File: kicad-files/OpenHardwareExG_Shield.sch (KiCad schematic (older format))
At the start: 196 parts, among them K1 CONN_3, P1 CONN_1, P10 CONN_10X2, P11 CONN_1, P12 CONN_1, P13 CONN_1, P14 CONN_1, P15 CONN_1, P16 CONN_1, P17 CONN_1, P18 CONN_1, P19 ARDUINO_SHIELD, P2 CONN_1, P20 CONN_3X2, P21 CONN_3X2, P22 CONN_4, P23 CONN_1, P24 CONN_1, P25 CONN_1, P26 CONN_1, P27 CONN_1, P28 CONN_1, P29 CONN_1, P3 CONN_1, P30 CONN_1, P31 CONN_1, P32 CONN_1, P33 CONN_1, P34 CONN_1, P35 CONN_1, P36 CONN_1, P37 CONN_1, P38 CONN_1, P39 CONN_1, P4 CONN_1, P40 CONN_1, P41 CONN_1, P42 CONN_1, P43 CONN_1, P44 CONN_1, P45 CONN_1, P46 CONN_1, P47 CONN_1, P48 CONN_1, P49 CONN_1, P5 CONN_1, P50 CONN_1, P51 CONN_1, P52 CONN_1, P53 CONN_1, P54 CONN_1, P55 CONN_1, P6 CONN_1, P7 CONN_1, P8 CONN_1, P9 CONN_1, U1 ADS1299, U2 BT1308W-600D, U3 TL431BIDBZR, U4 NI, U5 ADUM6000, U6 SI8663, U7 74LS02, U8 74LS00, U9 74LS125

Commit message: starting to choose footprints
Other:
- note added: "Analog Test Points"
- moved on the sheet: P1, P11, P12, P13, P14, P15, P16, P17, P18, P2, P3, P4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

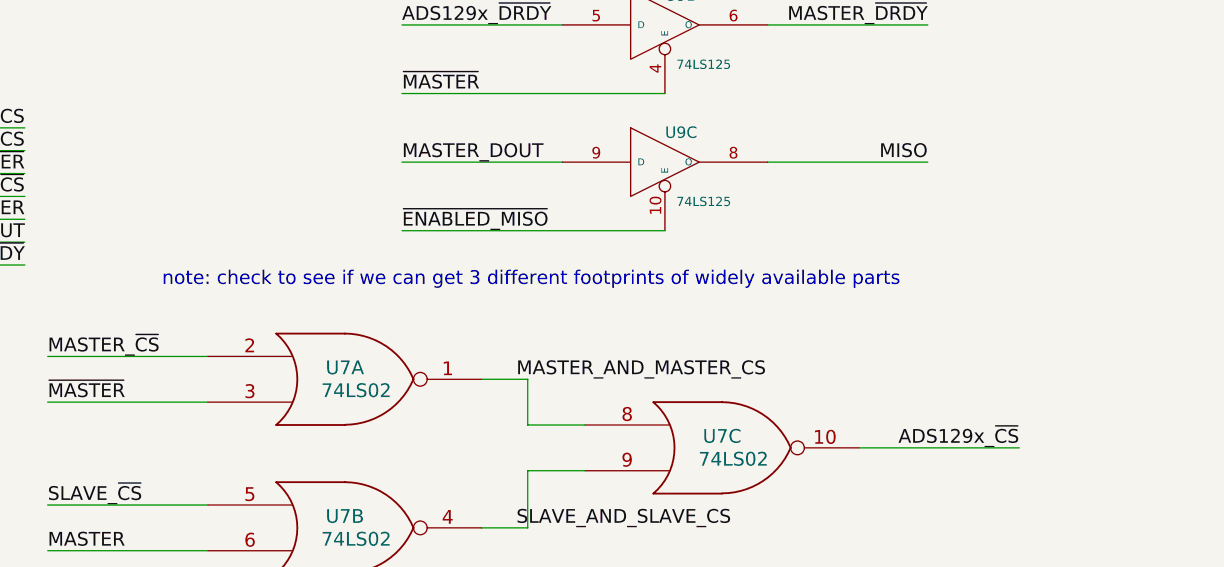
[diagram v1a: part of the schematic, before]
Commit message: add footprints for SMD headers and pogopads
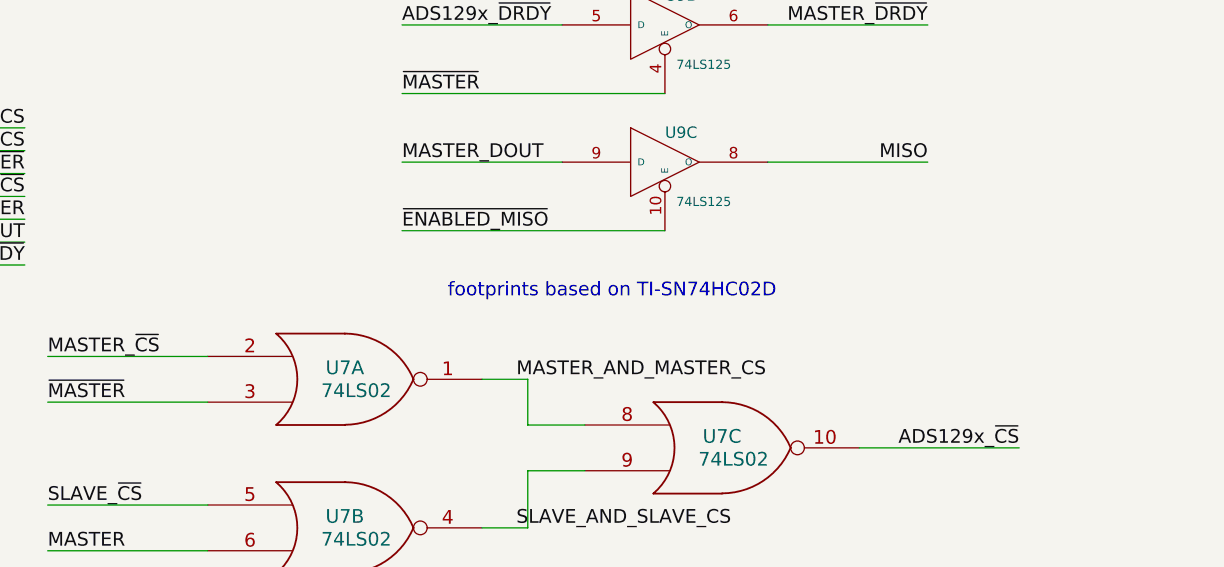
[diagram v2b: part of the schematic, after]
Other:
- note added: "footprints based on TI-SN74HC02D"
- note removed: "note: check to see if we can get 3 different footprints of widely available parts"
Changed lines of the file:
@@
 	1    0    0    -1
 $EndComp
-Text Notes 27600 8200 0    60   ~ 0
-note: check to see if we can get 3 different footprints of widely available parts
 $Comp
 L VCC #PWR069
@@
 Text Notes 23750 9550 2    60   ~ 0
 Analog Test Points
+Text Notes 28850 8250 0    60   ~ 0
+footprints based on TI-SN74HC02D
 $EndSCHEMATC

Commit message: add footprints to schematics
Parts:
- C1, C10, C11, C12, C13, C14, C15, C16, C17, C18, C19, C2, C20, C21, C22, C23, C24, C25, C26, C27, C28, C29, C3, C30, C31, C32, C33, C34, C4, C5, C6, C7, C8, C9, R1, R10, R11, R12, R13, R14, R15, R16, R17, R18, R19, R2, R20, R21, R22, R23, R24, R25, R26, R27, R28, R29, R3, R30, R31, R32, R33, R34, R4, R5, R6, R7, R8, R9: footprint SM0603 -> SM0805
- C52, C56: footprint ~ -> SM0805
- K1: footprint (none) -> PIN_ARRAY_3X1
- P1, P11, P12, P13, P14, P15, P16, P17, P18, P2, P22, P23, P24, P25, P26, P27, P28, P29, P3, P30, P31, P32, P33, P34, P35, P36, P37, P38, P39, P4, P40, P41, P42, P43, P44, P45, P46, P47, P48, P49, P5, P50, P51, P52, P53, P54, P55, P6, P7, P8, P9: footprint (none) -> POGO_PAD
- P10: footprint (none) -> pin_array_10x2
- P20: footprint (none) -> 54202-G0803ALF
- P21: footprint (none) -> 89898-303LF
- R40, R43, R44, R45: footprint ~ -> SM0603
- U4: footprint (none) -> SOT23
- U5: footprint (none) -> SO16W
- U6: footprint ~ -> SO16W
- U7, U8, U9: footprint ~ -> SO14E

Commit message: update notes, footprints on schematic
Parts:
- P22: footprint POGO_PAD -> PIN_ARRAY_4x1
- renumbered K1 to P56
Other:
- note added: "For 5V\n(required by ADS1299)\nuse 873-AAT3220IGY-33T1\nand 10uF capacitors\nand remove 0 Ohm resistor"
- note added: "Note: For 5.5V Crowbar circuit\nR42 should be 8.45k Ohms"
- note removed: "For 5V\n(required by ADS1299)\nuse NCP1117LPST33T3G\nand 10uF capacitors\nand remove 0 Ohm resistor"
- note removed: "Note: For 5.5V Crowbar circuit\nR65 should be 8.45k Ohms"

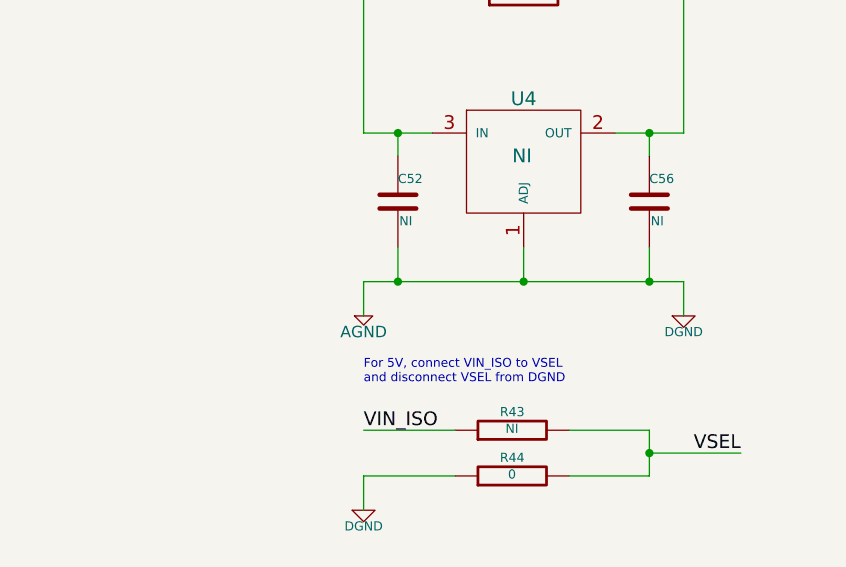
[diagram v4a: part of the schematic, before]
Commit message: start actually laying out the board
Added a 0 Ohm resistor to clarify the star-grounding of AGND and DGND,
we will likely remove this later.
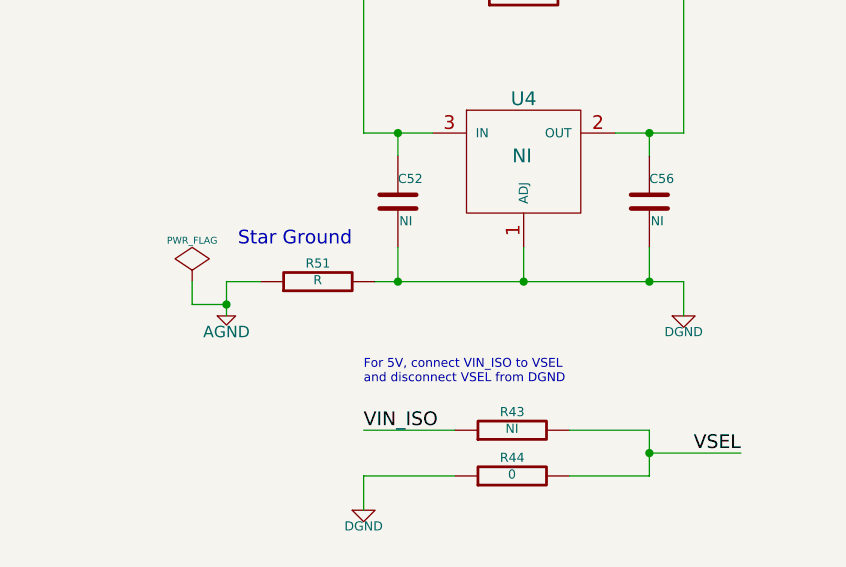
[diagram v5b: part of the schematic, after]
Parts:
- added R51: R, ~, symbol R
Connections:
- wire segments 617 -> 620
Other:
- note added: "Star Ground"

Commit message: checkpoint: untangle isolated/non-isolated rats-nest
Also, remove resistors from data lines which are now short.
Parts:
- removed R37, R38, R47, R48, R49, R50: 47, SM0603, symbol R
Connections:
- wire segments 620 -> 770

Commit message: checkpoint: layout analog capacitors
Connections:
- wire segments 770 -> 614

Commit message: initial layout of filter resistors and capacitors
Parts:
- C1, C10, C11, C12, C13, C14, C15, C16, C17, C18, C19, C2, C20, C21, C22, C23, C24, C25, C26, C27, C28, C29, C3, C30, C31, C32, C33, C34, C4, C5, C6, C7, C8, C9, R1, R10, R11, R12, R13, R14, R15, R16, R17, R18, R19, R2, R20, R21, R22, R23, R24, R25, R26, R27, R28, R29, R3, R30, R31, R32, R33, R34, R4, R5, R6, R7, R8, R9: footprint SM0805 -> SM0603
- R51: footprint ~ -> SM0603
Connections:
- wire segments 614 -> 617
